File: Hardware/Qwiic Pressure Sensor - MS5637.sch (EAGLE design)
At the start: 20 parts, among them J2 SMD, J3 PTH, J4 SMD, U1 MS5637

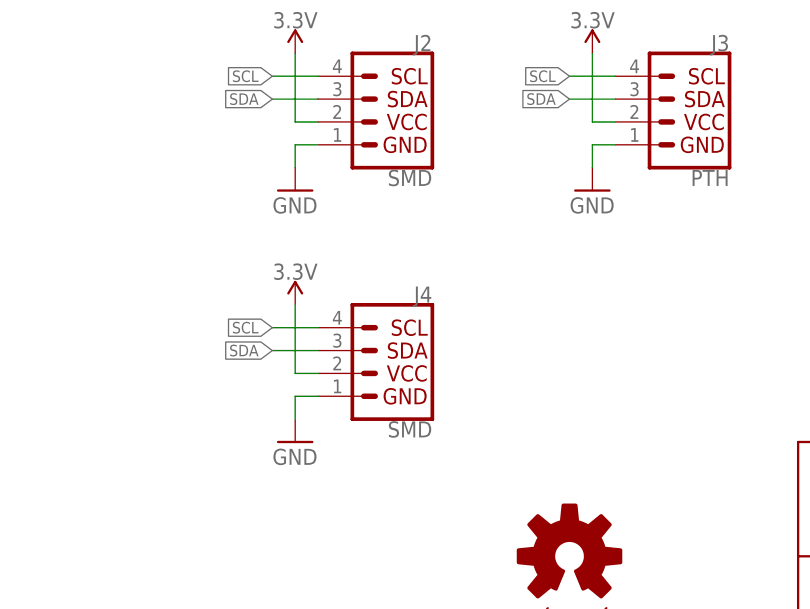
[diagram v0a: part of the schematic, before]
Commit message: Adding datasheet. Adding readme.
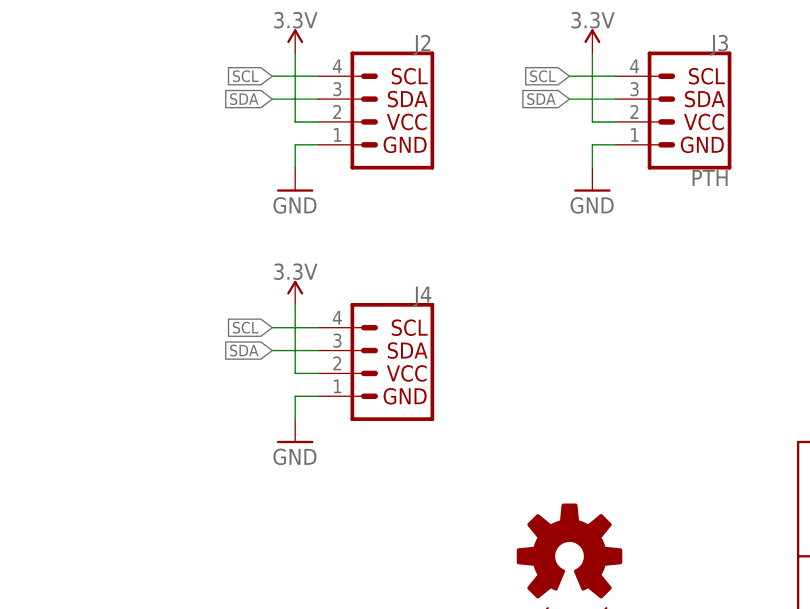
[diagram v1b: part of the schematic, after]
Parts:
- J2, J4: value SMD -> (none); device SparkX:I2C_STANDARDJS-1MM -> SparkFun-Connectors:I2C_STANDARDQWIIC
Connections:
- net 3.3V: now also J2.2, J4.2; no longer J2.VCC, J4.VCC
- net GND: now also J2.1, J4.1; no longer J2.GND, J4.GND
- net SCL: now also J2.4, J4.4; no longer J2.SCL, J4.SCL
- net SDA: now also J2.3, J4.3; no longer J2.SDA, J4.SDA
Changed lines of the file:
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@@
 <layer number="59" name="tCarbon" color="7" fill="1" visible="no" active="no"/>
 <layer number="60" name="bCarbon" color="7" fill="1" visible="no" active="no"/>
+<layer number="88" name="SimResults" color="9" fill="1" visible="yes" active="yes"/>
+<layer number="89" name="SimProbes" color="9" fill="1" visible="yes" active="yes"/>
 <layer number="90" name="Modules" color="5" fill="1" visible="no" active="no"/>
 <layer number="91" name="Nets" color="2" fill="1" visible="yes" active="yes"/>
@@
 <part name="SUPPLY5" library="SparkFun-PowerSymbols" deviceset="3.3V" device=""/>
 <part name="GND4" library="SparkFun" deviceset="GND" device=""/>
-<part name="J2" library="SparkX" deviceset="I2C_STANDARD" device="JS-1MM" value="SMD"/>
+<part name="J2" library="SparkFun-Connectors" deviceset="I2C_STANDARD" device="QWIIC"/>
 <part name="GND6" library="SparkFun" deviceset="GND" device=""/>
 <part name="SUPPLY7" library="SparkFun-PowerSymbols" deviceset="3.3V" device=""/>
@@
 <part name="C4" library="SparkFun-Capacitors" deviceset="0.1UF" device="-0603-25V-(+80/-20%)" value="0.1uF"/>
 <part name="SUPPLY8" library="SparkFun-PowerSymbols" deviceset="3.3V" device=""/>
-<part name="J4" library="SparkX" deviceset="I2C_STANDARD" device="JS-1MM" value="SMD"/>
+<part name="J4" library="SparkFun-Connectors" deviceset="I2C_STANDARD" device="QWIIC"/>
 <part name="GND8" library="SparkFun" deviceset="GND" device=""/>
 <part name="LOGO1" library="SparkFun-Aesthetics" deviceset="OSHW-LOGO" device="MINI"/>
@@
 </segment>
 <segment>
-<pinref part="J2" gate="G$1" pin="VCC"/>
+<pinref part="J2" gate="G$1" pin="2"/>
 <wire x1="93.98" y1="71.12" x2="91.44" y2="71.12" width="0.1524" layer="91"/>
 <wire x1="91.44" y1="71.12" x2="91.44" y2="78.74" width="0.1524" layer="91"/>
@@
 </segment>
 <segment>
-<pinref part="J4" gate="G$1" pin="VCC"/>
+<pinref part="J4" gate="G$1" pin="2"/>
 <wire x1="93.98" y1="43.18" x2="91.44" y2="43.18" width="0.1524" layer="91"/>
 <wire x1="91.44" y1="43.18" x2="91.44" y2="50.8" width="0.1524" layer="91"/>
@@
 </segment>
 <segment>
-<pinref part="J2" gate="G$1" pin="GND"/>
+<pinref part="J2" gate="G$1" pin="1"/>
 <wire x1="93.98" y1="68.58" x2="91.44" y2="68.58" width="0.1524" layer="91"/>
 <wire x1="91.44" y1="68.58" x2="91.44" y2="66.04" width="0.1524" layer="91"/>
@@
 </segment>
 <segment>
-<pinref part="J4" gate="G$1" pin="GND"/>
+<pinref part="J4" gate="G$1" pin="1"/>
 <wire x1="93.98" y1="40.64" x2="91.44" y2="40.64" width="0.1524" layer="91"/>
 <wire x1="91.44" y1="40.64" x2="91.44" y2="38.1" width="0.1524" layer="91"/>
@@
 <net name="SCL" class="0">
 <segment>
-<pinref part="J2" gate="G$1" pin="SCL"/>
+<pinref part="J2" gate="G$1" pin="4"/>
 <wire x1="93.98" y1="76.2" x2="88.9" y2="76.2" width="0.1524" layer="91"/>
 <label x="88.9" y="76.2" size="1.27" layer="95" rot="R180" xref="yes"/>
@@
 </segment>
 <segment>
-<pinref part="J4" gate="G$1" pin="SCL"/>
+<pinref part="J4" gate="G$1" pin="4"/>
 <wire x1="93.98" y1="48.26" x2="88.9" y2="48.26" width="0.1524" layer="91"/>
 <label x="88.9" y="48.26" size="1.27" layer="95" rot="R180" xref="yes"/>
@@
 <net name="SDA" class="0">
 <segment>
-<pinref part="J2" gate="G$1" pin="SDA"/>
+<pinref part="J2" gate="G$1" pin="3"/>
 <wire x1="93.98" y1="73.66" x2="88.9" y2="73.66" width="0.1524" layer="91"/>
 <label x="88.9" y="73.66" size="1.27" layer="95" rot="R180" xref="yes"/>
@@
 </segment>
 <segment>
-<pinref part="J4" gate="G$1" pin="SDA"/>
+<pinref part="J4" gate="G$1" pin="3"/>
 <wire x1="93.98" y1="45.72" x2="88.9" y2="45.72" width="0.1524" layer="91"/>
 <label x="88.9" y="45.72" size="1.27" layer="95" rot="R180" xref="yes"/>
